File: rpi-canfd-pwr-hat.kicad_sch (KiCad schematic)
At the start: 82 parts, among them J1 Conn_01x02, J2 Conn_01x04_Pin, J3 Raspberry_Pi, J4 Conn_01x02, J5 Conn_01x02, U1 XC6206P332MR, U2 LM73100, U3 TPS259472A, U4 XC6206P182MR, U5 TPS56637, U6 ICM-20948, U7 CAT24C256, U8 MCP2518FD, U9 TCAN3413, Y1 48M

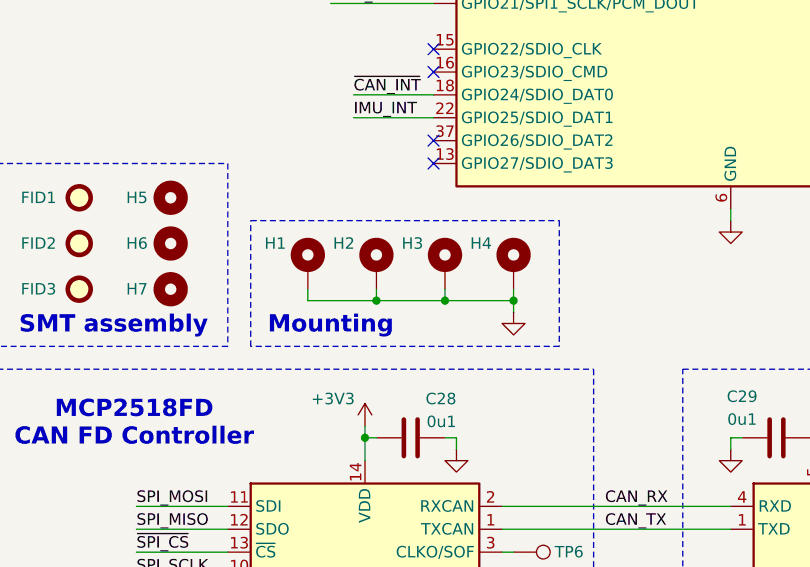
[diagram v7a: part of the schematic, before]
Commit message: pcb: update board outline
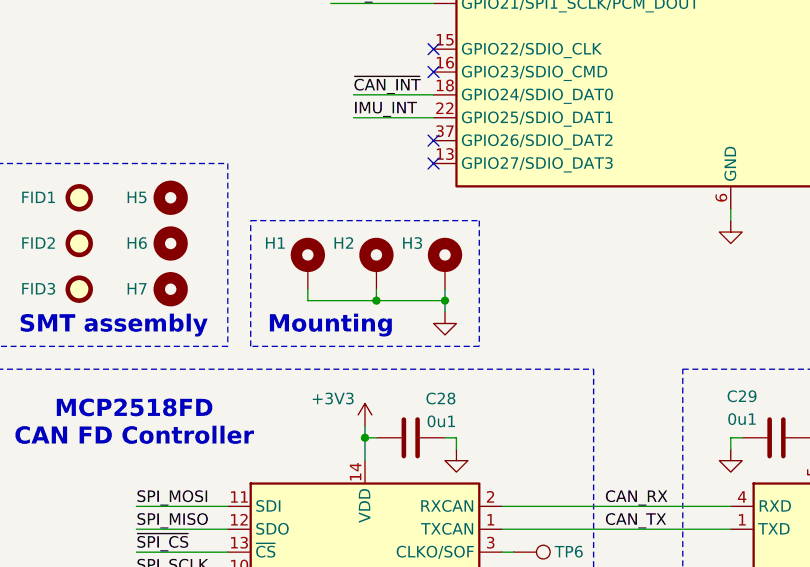
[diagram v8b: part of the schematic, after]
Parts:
- removed H3: MountingHole_Pad, MountingHole:MountingHole_2.7mm_M2.5_Pad_Via, symbol Mechanical:MountingHole_Pad
- renumbered H4 to H3
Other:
- moved on the sheet: H3
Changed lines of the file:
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@@
 	(rectangle
 		(start 177.8 97.79)
-		(end 212.09 111.76)
+		(end 203.2 111.76)
 		(stroke
 			(width 0)
@@
 	)
 	(junction
-		(at 207.01 106.68)
-		(diameter 0)
-		(color 0 0 0 0)
-	)
-	(junction
 		(at 76.2 30.48)
 		(diameter 0)
@@
 	(wire
 		(pts
-			(xy 207.01 106.68) (xy 207.01 107.95)
+			(xy 199.39 106.68) (xy 199.39 107.95)
 		)
 		(stroke
@@
 	(wire
 		(pts
-			(xy 207.01 105.41) (xy 207.01 106.68)
-		)
-		(stroke
-			(width 0)
-			(type default)
-		)
-	)
-	(wire
-		(pts
 			(xy 114.3 104.14) (xy 113.03 104.14)
 		)
@@
 	(wire
 		(pts
-			(xy 191.77 106.68) (xy 207.01 106.68)
+			(xy 191.77 106.68) (xy 199.39 106.68)
 		)
 		(stroke
@@
 	)
 	(symbol
-		(lib_id "Mechanical:MountingHole_Pad")
-		(at 199.39 102.87 0)
-		(unit 1)
-		(body_style 1)
-		(exclude_from_sim no)
-		(in_bom no)
-		(on_board yes)
-		(in_pos_files yes)
-		(dnp no)
-		(property "Reference" "H3"
-			(at 194.564 100.33 0)
-			(show_name no)
-			(do_not_autoplace no)
-			(effects
-				(font
-					(size 1.27 1.27)
-				)
-				(justify left)
-			)
-		)
-		(property "Value" "MountingHole_Pad"
-			(at 203.2 101.6 90)
-			(hide yes)
-			(show_name no)
-			(do_not_autoplace no)
-			(effects
-				(font
-					(size 1.27 1.27)
-				)
-			)
-		)
-		(property "Footprint" "MountingHole:MountingHole_2.7mm_M2.5_Pad_Via"
-			(at 199.39 102.87 0)
-			(hide yes)
-			(show_name no)
-			(do_not_autoplace no)
-			(effects
-				(font
-					(size 1.27 1.27)
-				)
-			)
-		)
-		(property "Datasheet" ""
-			(at 199.39 102.87 0)
-			(hide yes)
-			(show_name no)
-			(do_not_autoplace no)
-			(effects
-				(font
-					(size 1.27 1.27)
-				)
-			)
-		)
-		(property "Description" "Mounting Hole with connection"
-			(at 199.39 102.87 0)
-			(hide yes)
-			(show_name no)
-			(do_not_autoplace no)
-			(effects
-				(font
-					(size 1.27 1.27)
-				)
-			)
-		)
-		(pin "1"
-		)
-		(instances
-			(project "rpi-canfd-pwr-hat"
-				(path "/35b6363d-fbe9-4c33-b2ab-05d20bd8dec5"
-					(reference "H3")
-					(unit 1)
-				)
-			)
-		)
-	)
-	(symbol
 		(lib_id "Device:C")
 		(at 111.76 168.91 0)
@@
 	(symbol
 		(lib_id "Mechanical:MountingHole_Pad")
-		(at 207.01 102.87 0)
+		(at 199.39 102.87 0)
 		(unit 1)
 		(body_style 1)
@@
 		(in_pos_files yes)
 		(dnp no)
-		(property "Reference" "H4"
-			(at 202.184 100.33 0)
+		(property "Reference" "H3"
+			(at 194.564 100.33 0)
 			(show_name no)
 			(do_not_autoplace no)
@@
 		)
 		(property "Value" "MountingHole_Pad"
-			(at 210.82 101.6 90)
+			(at 203.2 101.6 90)
 			(hide yes)
 			(show_name no)
@@
 		)
 		(property "Footprint" "MountingHole:MountingHole_2.7mm_M2.5_Pad_Via"
-			(at 207.01 102.87 0)
+			(at 199.39 102.87 0)
 			(hide yes)
 			(show_name no)
@@
 		)
 		(property "Datasheet" ""
-			(at 207.01 102.87 0)
+			(at 199.39 102.87 0)
 			(hide yes)
 			(show_name no)
@@
 		)
 		(property "Description" "Mounting Hole with connection"
-			(at 207.01 102.87 0)
+			(at 199.39 102.87 0)
 			(hide yes)
 			(show_name no)
@@
 			(project "rpi-canfd-pwr-hat"
 				(path "/35b6363d-fbe9-4c33-b2ab-05d20bd8dec5"
-					(reference "H4")
+					(reference "H3")
 					(unit 1)
 				)
@@
 	(symbol
 		(lib_id "power:GND")
-		(at 207.01 107.95 0)
+		(at 199.39 107.95 0)
 		(unit 1)
 		(body_style 1)
@@
 		(dnp no)
 		(property "Reference" "#PWR0130"
-			(at 207.01 114.3 0)
+			(at 199.39 114.3 0)
 			(hide yes)
 			(show_name no)
@@
 		)
 		(property "Value" "GND"
-			(at 206.756 112.522 0)
+			(at 199.136 112.522 0)
 			(hide yes)
 			(show_name no)
@@
 		)
 		(property "Footprint" ""
-			(at 207.01 107.95 0)
+			(at 199.39 107.95 0)
 			(hide yes)
 			(show_name no)
@@
 		)
 		(property "Datasheet" ""
-			(at 207.01 107.95 0)
+			(at 199.39 107.95 0)
 			(hide yes)
 			(show_name no)
@@
 		)
 		(property "Description" "Power symbol creates a global label with name \"GND\" , ground"
-			(at 207.01 107.95 0)
+			(at 199.39 107.95 0)
 			(hide yes)
 			(show_name no)
